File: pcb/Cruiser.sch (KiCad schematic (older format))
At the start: 43 parts

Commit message: preliminary 25mm x 50mm rectangular PCB layout completed.
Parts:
- removed P?: Fuel Pump, symbol CONN_1
- removed P?: AN0-15, symbol CONN_16
- removed P?: CONN_6, symbol CONN_6
- removed P?: PK0-3, symbol CONN_4
- removed P?: PB0-7, symbol CONN_8
- removed P?: PK4&5, symbol CONN_2
- removed P?: PT0-7, symbol CONN_8
- removed P?: PP0-7, symbol CONN_8
- removed P?: TXCAN0, symbol CONN_1
- removed P?: RXCAN0, symbol CONN_1
- removed P?: TX1, symbol CONN_1
- removed P?: RX1, symbol CONN_1
- removed P?: 5v, symbol CONN_1
- removed P?: GND, symbol CONN_1
- gave numbers to parts that had none: 29
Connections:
- wire segments 190 -> 101
- no-connect marks 30 -> 87

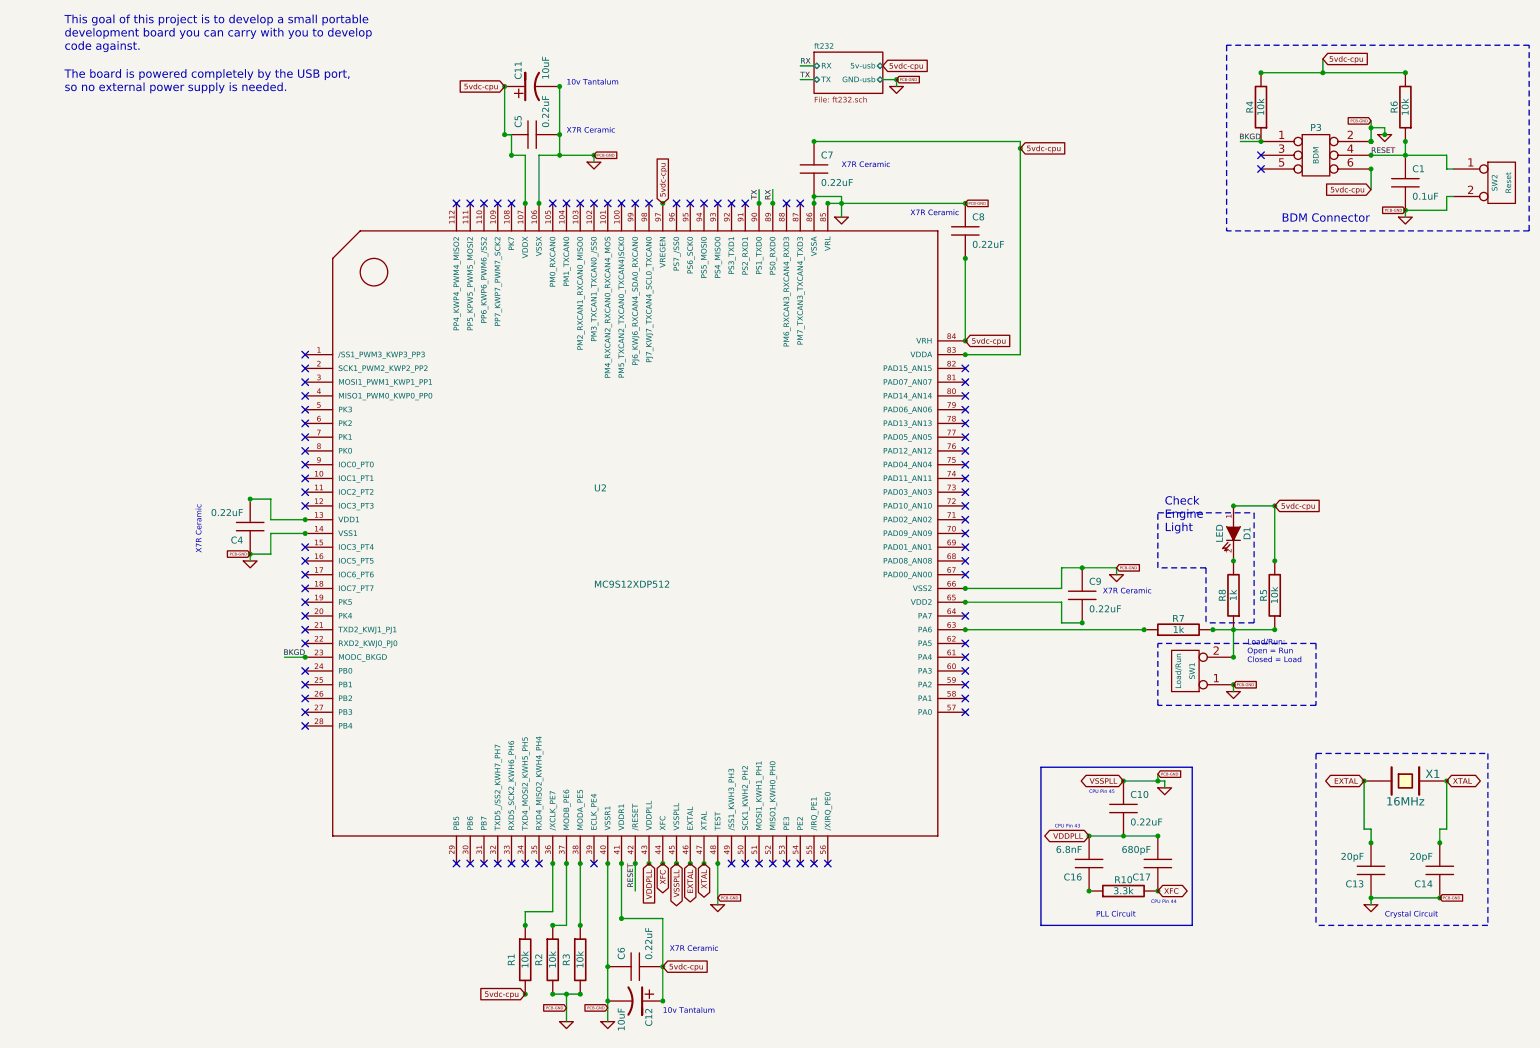
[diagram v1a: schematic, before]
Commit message: Condensed the schematic to one sheet for easier reading.
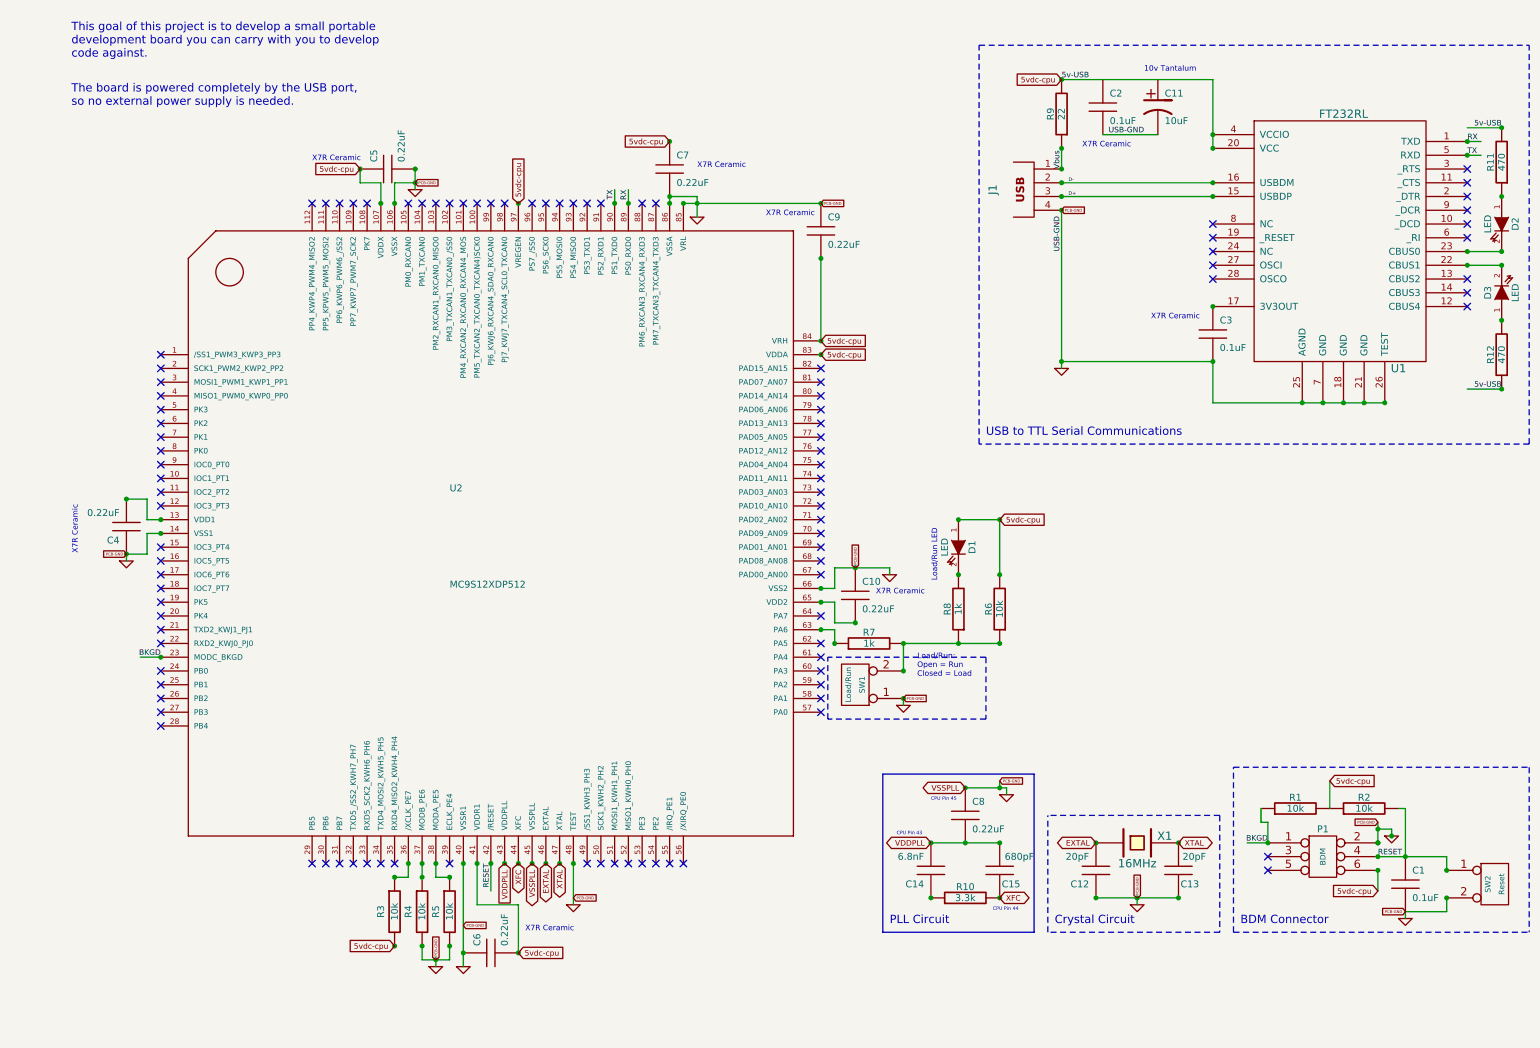
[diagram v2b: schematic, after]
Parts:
- removed C12: 10uF, symbol CP1
- added C2, C3: 0.1uF, symbol C
- added D2, D3: LED, symbol LED
- added J1: USB-A, symbol USB_2
- added R11, R12: 470, symbol R
- added R9: 22, symbol R
- added U1: FT232RL, symbol FT232RL
- renumbered C9 to C10, C13 to C12, C14 to C13, C16 to C14, C17 to C15, C10 to C8, C8 to C9, P3 to P1, R4 to R1, R6 to R2, R1 to R3, R2 to R4, R3 to R5, R5 to R6
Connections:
- net labels added: 5v-USB, D+, D-, USB-GND, Vbus
- wire segments 101 -> 106
- no-connect marks 87 -> 101
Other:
- note added: "Load/Run LED"
- note added: "USB to TTL Serial Communications"
- note removed: "10v Tantalum\n"
- note removed: "Check\nEngine\nLight"
- moved on the sheet: C1, C10, C12, C13, C14, C15, C4, C5, C6, C7, C8, C9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

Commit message: Updated git hash on schematics to 957894db06
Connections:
- wire segments 106 -> 88
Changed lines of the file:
@@
-EESchema Schematic File Version 2  date Sun 04 Nov 2012 10:52:01 AM EST
+EESchema Schematic File Version 2  date Sun 04 Nov 2012 10:56:37 AM EST
 LIBS:opto
 LIBS:Jaguar
@@
 Date "4 nov 2012"
 Rev "0.1-alpha"
-Comp "git hash: "
+Comp "git hash: 957894db06"
 Comment1 ""
 Comment2 ""
@@
 	9000 7000 11150 7000
 Wire Wire Line
-	7750 2900 7750 2850
-Wire Wire Line
-	7750 2850 7750 1750
+	7750 2900 7750 1750
 Wire Wire Line
 	10950 1150 10700 1150
@@
 	8900 6150 8900 7000
 Wire Wire Line
-	8000 6750 8300 6750
-Wire Wire Line
-	8300 6750 8600 6750
+	8000 6750 8600 6750
 Connection ~ 2900 7100
 Connection ~ 2900 6600
@@
 	3300 7100 3300 7200
 Wire Wire Line
-	3300 7200 3200 7200
-Wire Wire Line
-	3200 7200 3100 7200
+	3300 7200 3100 7200
 Wire Wire Line
 	3100 7200 3100 7100
@@
 	10550 6550 10550 6450
 Wire Wire Line
-	10550 6450 10250 6450
-Wire Wire Line
-	10250 6450 10050 6450
+	10550 6450 10050 6450
 Connection ~ 6000 2100
 Connection ~ 6000 1700
@@
 	6100 4500 6100 4350
 Wire Wire Line
-	6100 4350 6250 4350
-Wire Wire Line
-	6250 4350 6500 4350
+	6100 4350 6500 4350
 Wire Wire Line
 	950  3850 1100 3850
@@
 	7350 6000 7350 5950
 Wire Wire Line
-	7350 5950 7300 5950
-Wire Wire Line
-	7300 5950 7050 5950
+	7350 5950 7050 5950
 Connection ~ 3050 1550
 Wire Wire Line
@@
 Connection ~ 10050 6350
 Wire Wire Line
-	6800 6350 7050 6350
-Wire Wire Line
-	7050 6350 7300 6350
+	6800 6350 7300 6350
 Wire Wire Line
 	1100 3850 1100 4000
@@
 Connection ~ 7300 5950
 Wire Wire Line
-	5100 1650 5100 1700
-Wire Wire Line
-	5100 1700 5100 1800
-Wire Wire Line
-	6000 1700 5100 1700
-Wire Wire Line
-	5100 1700 5000 1700
+	5100 1650 5100 1800
+Wire Wire Line
+	6000 1700 5000 1700
 Wire Wire Line
 	2900 1550 3050 1550
@@
 Connection ~ 4900 1250
 Wire Wire Line
-	10050 6350 10050 6250
-Wire Wire Line
-	10050 6250 10050 6200
+	10050 6350 10050 6200
 Connection ~ 10050 6250
 Wire Wire Line
-	3050 1600 3050 1550
-Wire Wire Line
-	3050 1550 3050 1450
+	3050 1600 3050 1450
 Wire Wire Line
 	3100 6500 3100 6600
@@
 Connection ~ 3200 7200
 Wire Wire Line
-	3400 6500 3400 7150
-Wire Wire Line
-	3400 7150 3400 7250
+	3400 6500 3400 7250
 Connection ~ 3400 7150
 Connection ~ 3800 7150
@@
 	9000 7000 9000 5800
 Wire Wire Line
-	6600 4900 7000 4900
-Wire Wire Line
-	7000 4900 7300 4900
+	6600 4900 7300 4900
 Connection ~ 7000 4900
 Connection ~ 7750 2850
@@
 Connection ~ 10700 1250
 Wire Wire Line
-	8850 3150 9500 3150
-Wire Wire Line
-	9500 3150 9650 3150
-Wire Wire Line
-	9650 3150 9800 3150
-Wire Wire Line
-	9800 3150 9950 3150
-Wire Wire Line
-	9950 3150 10100 3150
+	8850 3150 10100 3150
 Connection ~ 7750 800
 Connection ~ 7750 1300
@@
 	7750 800  8850 800
 Wire Wire Line
-	8850 800  8850 1200
-Wire Wire Line
-	8850 1200 8850 1300
+	8850 800  8850 1300
 Connection ~ 10950 2050
 Connection ~ 10950 1650
@@
 Crystal Circuit
 $Comp
-L GND #PWR5
+L GND #PWR01
 U 1 1 50954234
 P 3200 7250
-F 0 "#PWR5" H 3200 7250 30  0001 C CNN
+F 0 "#PWR01" H 3200 7250 30  0001 C CNN
 F 1 "GND" H 3200 7180 30  0001 C CNN
 	1    3200 7250
@@
 $EndComp
 $Comp
-L GND #PWR6
+L GND #PWR02
 U 1 1 50954233
 P 3400 7250
-F 0 "#PWR6" H 3400 7250 30  0001 C CNN
+F 0 "#PWR02" H 3400 7250 30  0001 C CNN
 F 1 "GND" H 3400 7180 30  0001 C CNN
 	1    3400 7250
@@
 $EndComp
 $Comp
-L GND #PWR10
+L GND #PWR03
 U 1 1 50954232
 P 8300 6800
-F 0 "#PWR10" H 8300 6800 30  0001 C CNN
+F 0 "#PWR03" H 8300 6800 30  0001 C CNN
 F 1 "GND" H 8300 6730 30  0001 C CNN
 	1    8300 6800
@@
 $EndComp
 $Comp
-L GND #PWR11
+L GND #PWR04
 U 1 1 50954231
 P 6500 4400
-F 0 "#PWR11" H 6500 4400 30  0001 C CNN
+F 0 "#PWR04" H 6500 4400 30  0001 C CNN
 F 1 "GND" H 6500 4330 30  0001 C CNN
 	1    6500 4400
@@
 $EndComp
 $Comp
-L GND #PWR12
+L GND #PWR05
 U 1 1 50954230
 P 6600 5350
-F 0 "#PWR12" H 6600 5350 30  0001 C CNN
+F 0 "#PWR05" H 6600 5350 30  0001 C CNN
 F 1 "GND" H 6600 5280 30  0001 C CNN
 	1    6600 5350
@@
 $EndComp
 $Comp
-L GND #PWR8
+L GND #PWR06
 U 1 1 5095422F
 P 5100 1800
-F 0 "#PWR8" H 5100 1800 30  0001 C CNN
+F 0 "#PWR06" H 5100 1800 30  0001 C CNN
 F 1 "GND" H 5100 1730 30  0001 C CNN
 	1    5100 1800
@@
 $EndComp
 $Comp
-L GND #PWR13
+L GND #PWR07
 U 1 1 5095422E
 P 7750 2900
-F 0 "#PWR13" H 7750 2900 30  0001 C CNN
+F 0 "#PWR07" H 7750 2900 30  0001 C CNN
 F 1 "GND" H 7750 2830 30  0001 C CNN
 	1    7750 2900
@@
 $EndComp
 $Comp
-L GND #PWR4
+L GND #PWR08
 U 1 1 5095422D
 P 3050 1600
-F 0 "#PWR4" H 3050 1600 30  0001 C CNN
+F 0 "#PWR08" H 3050 1600 30  0001 C CNN
 F 1 "GND" H 3050 1530 30  0001 C CNN
 	1    3050 1600
@@
 $EndComp
 $Comp
-L GND #PWR3
+L GND #PWR09
 U 1 1 5095422C
 P 10250 6900
-F 0 "#PWR3" H 10250 6900 30  0001 C CNN
+F 0 "#PWR09" H 10250 6900 30  0001 C CNN
 F 1 "GND" H 10250 6830 30  0001 C CNN
 	1    10250 6900
@@
 $EndComp
 $Comp
-L GND #PWR2
+L GND #PWR010
 U 1 1 5095422B
 P 10150 6300
-F 0 "#PWR2" H 10150 6300 30  0001 C CNN
+F 0 "#PWR010" H 10150 6300 30  0001 C CNN
 F 1 "GND" H 10150 6230 30  0001 C CNN
 	1    10150 6300
@@
 $EndComp
 $Comp
-L GND #PWR9
+L GND #PWR011
 U 1 1 5095422A
 P 7350 6000
-F 0 "#PWR9" H 7350 6000 30  0001 C CNN
+F 0 "#PWR011" H 7350 6000 30  0001 C CNN
 F 1 "GND" H 7350 5930 30  0001 C CNN
 	1    7350 6000
@@
 $EndComp
 $Comp
-L GND #PWR7
+L GND #PWR012
 U 1 1 50954229
 P 4200 6800
-F 0 "#PWR7" H 4200 6800 30  0001 C CNN
+F 0 "#PWR012" H 4200 6800 30  0001 C CNN
 F 1 "GND" H 4200 6730 30  0001 C CNN
 	1    4200 6800
@@
 $EndComp
 $Comp
-L GND #PWR1
+L GND #PWR013
 U 1 1 50954227
 P 950 4300
-F 0 "#PWR1" H 950 4300 30  0001 C CNN
+F 0 "#PWR013" H 950 4300 30  0001 C CNN
 F 1 "GND" H 950 4230 30  0001 C CNN
 	1    950  4300
